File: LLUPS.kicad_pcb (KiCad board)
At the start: 2 copper layers, 140 x 90 mm, 39 parts, among them J1 USB_C, J2 Output, J3 Debug, Q1 FS8205A, U1 USBLC6-2SC6, U2 BQ24072, U3 HY2113-KB5B, U4 MT3608, U5 AP2112K-3.3, U6 LN61CN3302MR-G

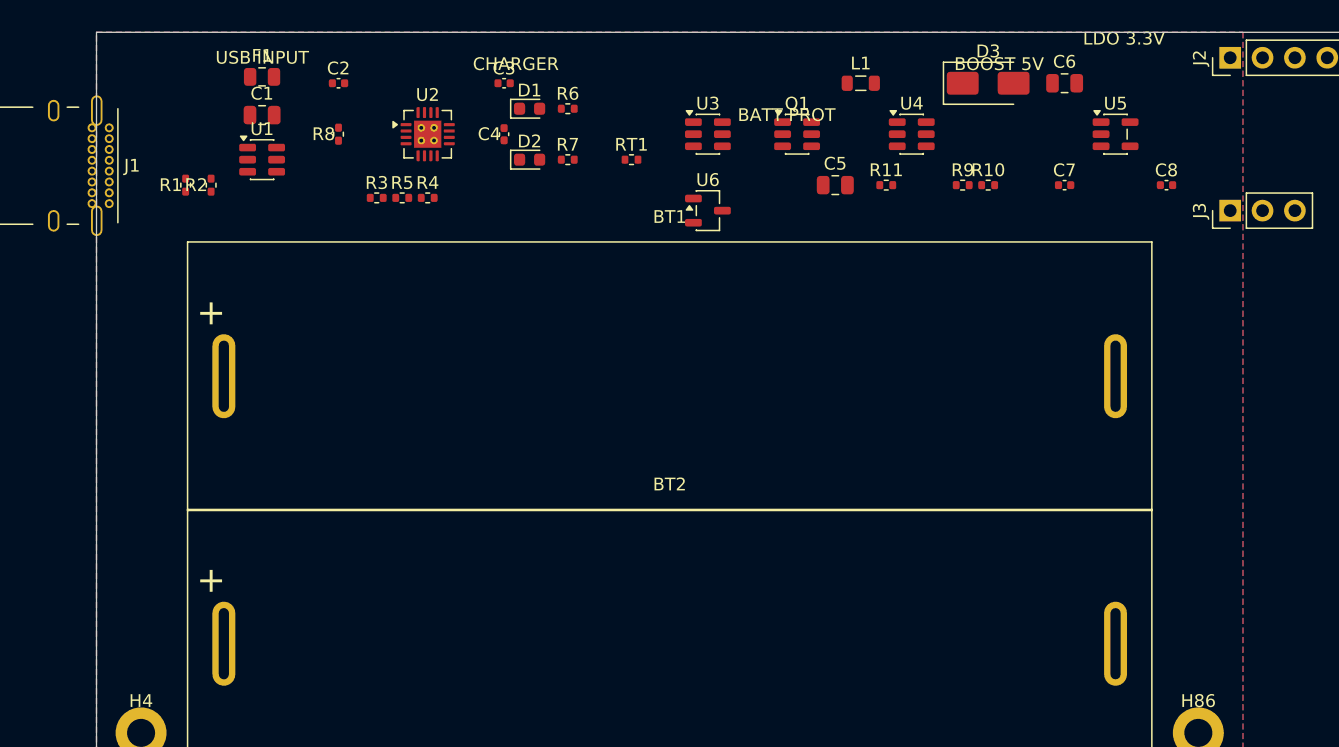
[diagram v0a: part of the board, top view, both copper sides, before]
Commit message: feat: add silkscreen functional block labels to PCB and update config
- Apply rounded-rect silkscreen outlines with group labels to LLUPS.kicad_pcb
- Add BT1 BATTERY entry to group_labels in LLUPS_autoplacer.json
- Update KiCraft submodule with full silkscreen pipeline support
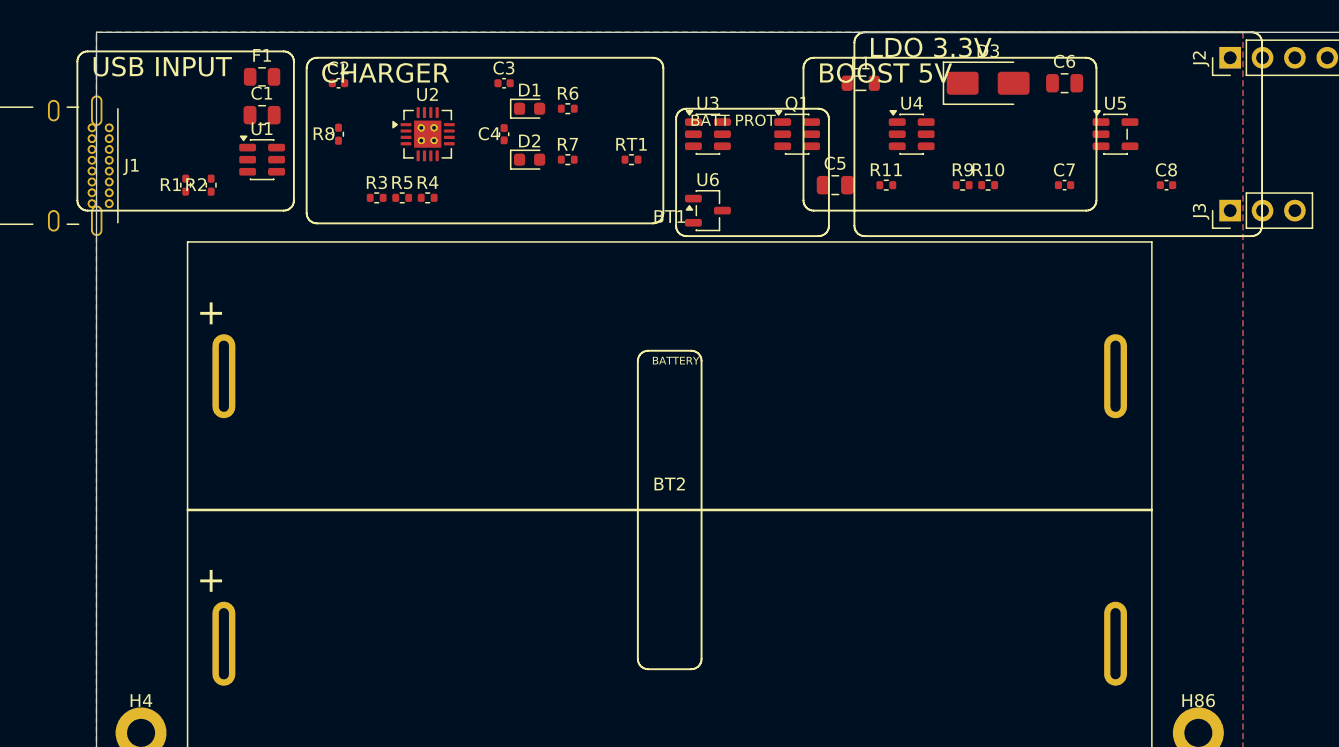
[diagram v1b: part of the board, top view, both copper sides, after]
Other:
- board text added: "BATTERY"
